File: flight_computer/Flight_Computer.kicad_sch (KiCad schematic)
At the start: 31 parts

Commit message: Update Flight_Computer.kicad_sch
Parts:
- added C?: 2.2uF, symbol Device:C
- added C? (x2): 22uF, symbol Device:C
- added D?: LED, symbol Device:LED
- added R?: 1ohm, symbol Device:R
- added R?: 1Kohm, symbol Device:R
- added R?: R, symbol Device:R
- added U?: AMS1117-3.3, Package_TO_SOT_SMD:SOT-223-3_TabPin2, symbol Regulator_Linear:AMS1117-3.3
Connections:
- net +3V3: now also C?.1, D?.2 (A), U?.2 (VO); no longer C?.1, C?.1, U?.1 (VBAT)
- net GND: now also C?.2, C?.2, R?.2, R?.2, U?.1 (GND)
- net at U?.22 (VCAP1): now also C?.2, R?.1
- net 3V3_Buck_input: no longer names the net of J?.A4 (VBUS), J?.A9 (VBUS), J?.B4 (VBUS), J?.B9 (VBUS)
- net 3V3_Buck_input: now also C?.1, U?.3 (VI)
- new net: D?.1 (K), R?.1
- new net: C?.1, R?.1, R?.2
- new net Buck_Output: C?.1, C?.1, U?.1 (VBAT)
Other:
- note added: "Find Rleak value"
- moved on the sheet: C?, Y?

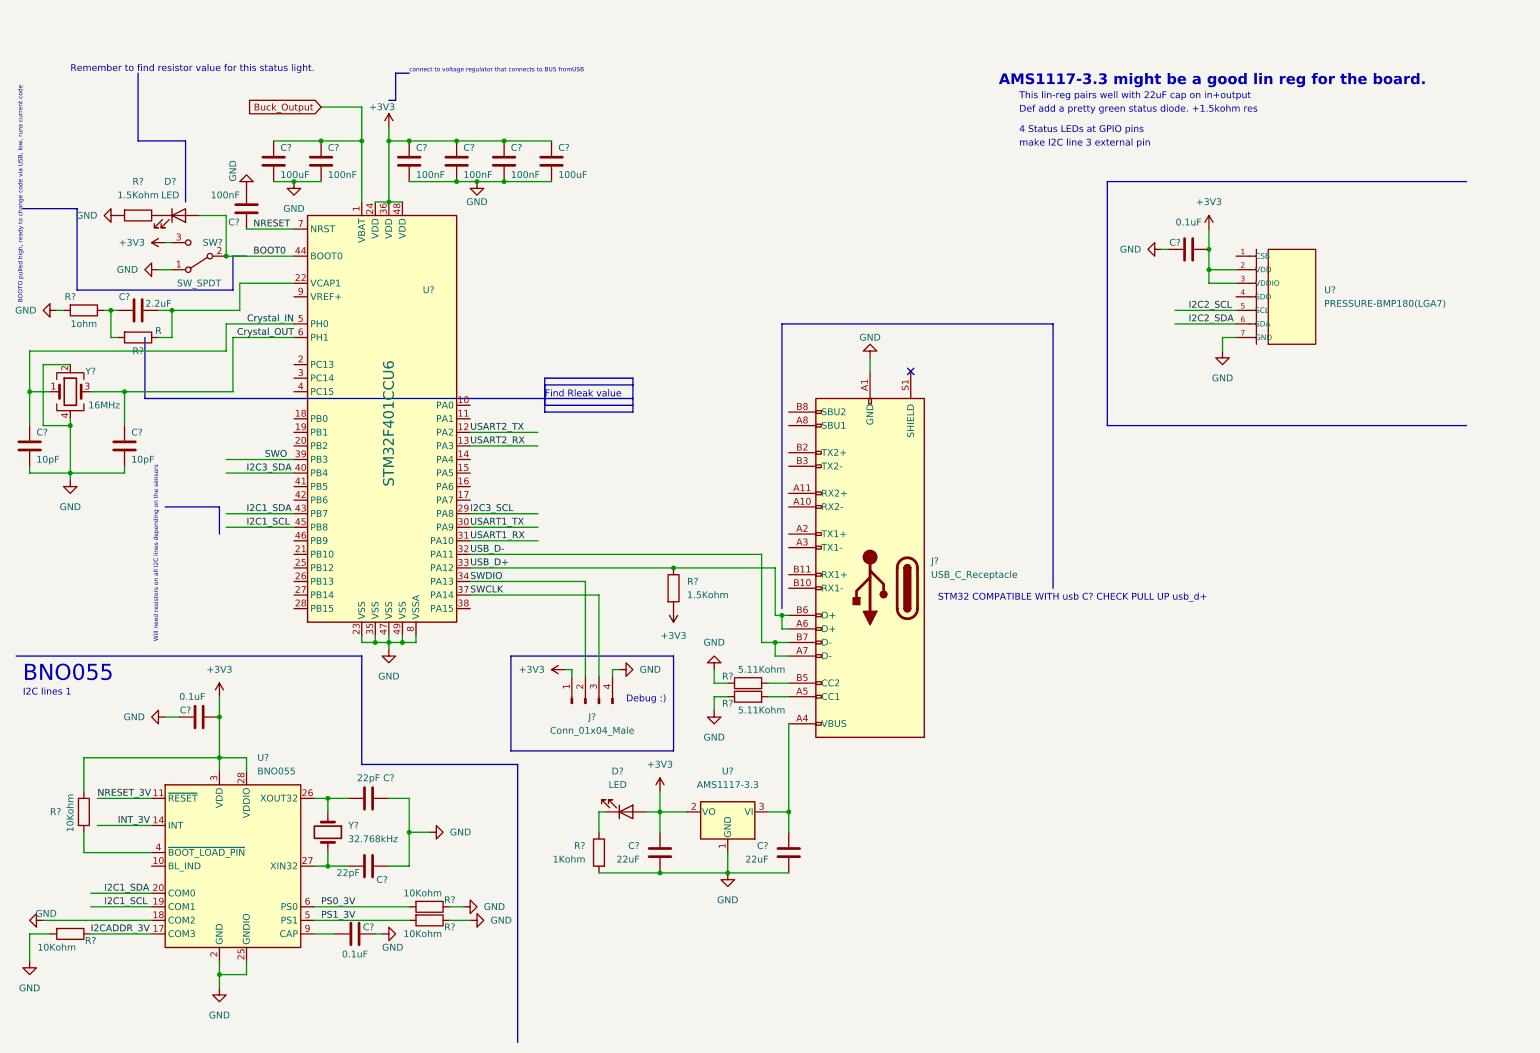
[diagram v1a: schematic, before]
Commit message: Revert "Update Flight_Computer.kicad_sch"
This reverts commit 00c3728efcfbe39ff6afe041c82bac8e4ccad5c9.
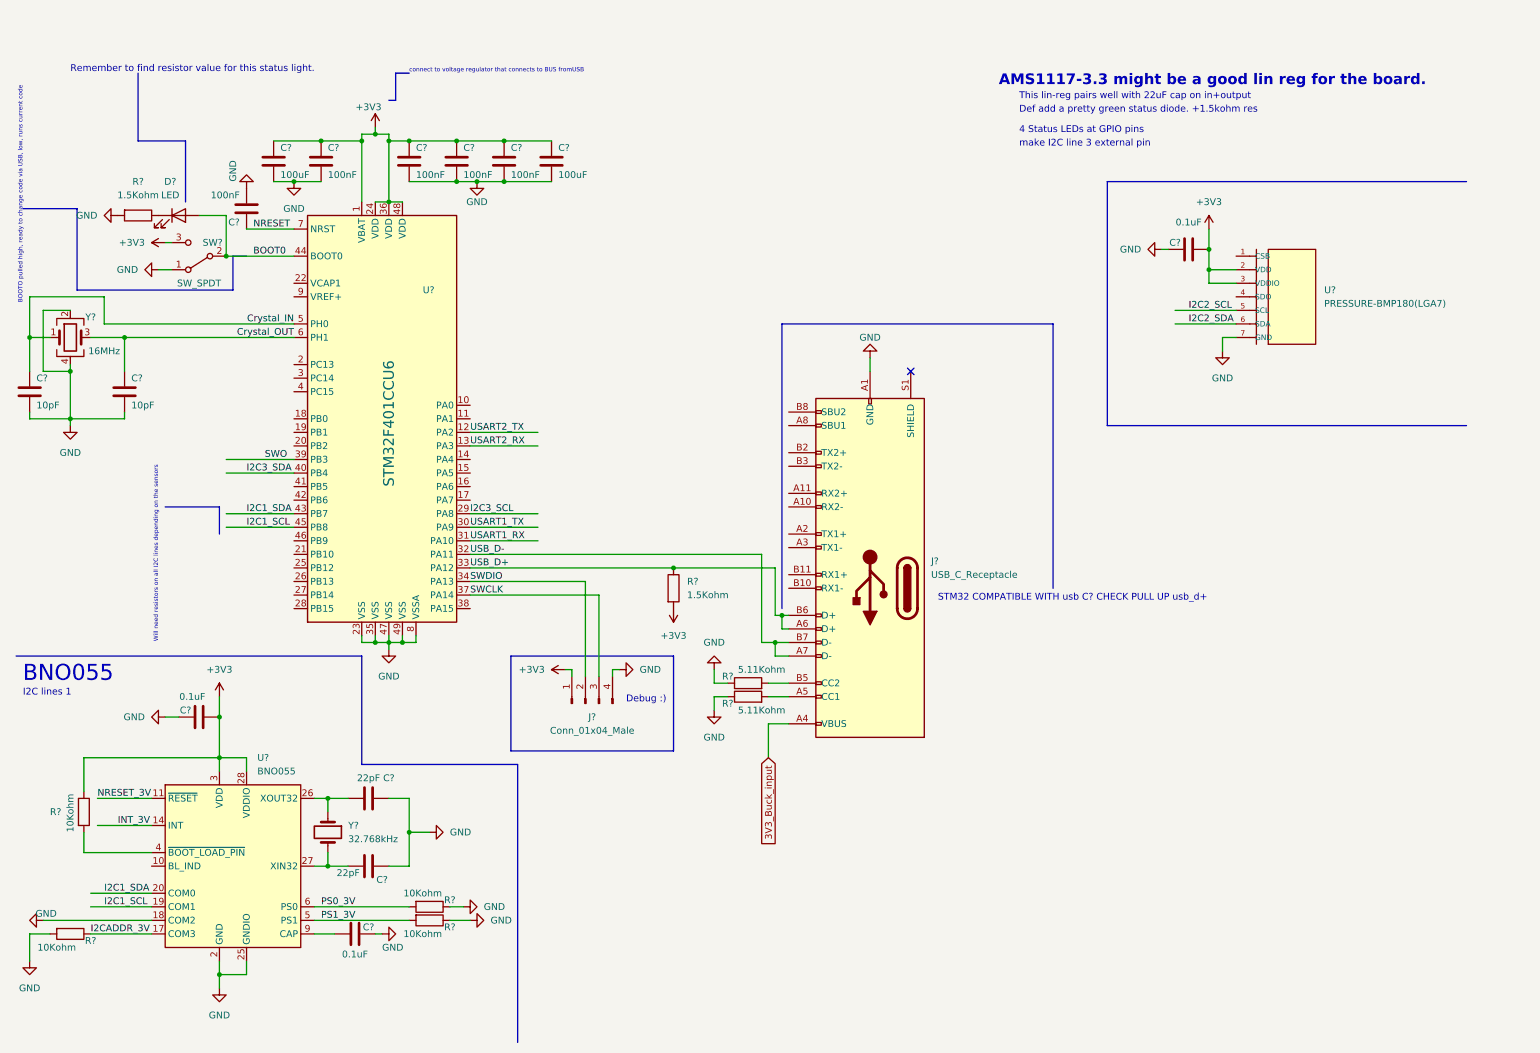
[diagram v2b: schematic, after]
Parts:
- removed C?: 2.2uF, symbol Device:C
- removed C? (x2): 22uF, symbol Device:C
- removed D?: LED, symbol Device:LED
- removed R?: 1ohm, symbol Device:R
- removed R?: 1Kohm, symbol Device:R
- removed R?: R, symbol Device:R
- removed U?: AMS1117-3.3, Package_TO_SOT_SMD:SOT-223-3_TabPin2, symbol Regulator_Linear:AMS1117-3.3
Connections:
- net Buck_Output is gone; now on net +3V3: C?.1, C?.1, U?.1 (VBAT)
- net 3V3_Buck_input: now reaches J?.A4 (VBUS), J?.A9 (VBUS), J?.B4 (VBUS), J?.B9 (VBUS)
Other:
- note removed: "Find Rleak value"
- moved on the sheet: C?, Y?

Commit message: Update Flight_Computer.kicad_sch
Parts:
- added J?: Conn_01x02_Male, symbol Connector:Conn_01x02_Male
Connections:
- net I2C3_SCL: now also J?.2 (Pin_2)
- net I2C3_SDA: now also J?.1 (Pin_1)
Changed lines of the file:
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@@
+    (stroke (width 0) (type default) (color 0 0 0 0))
+  )
+  (wire (pts (xy 111.76 92.71) (xy 111.76 97.79))
     (stroke (width 0) (type default) (color 0 0 0 0))
   )
@@
     (stroke (width 0) (type default) (color 0 0 0 0))
   )
+  (wire (pts (xy 110.49 90.17) (xy 119.38 90.17))
+    (stroke (width 0) (type default) (color 0 0 0 0))
+  )
   (wire (pts (xy 80.01 26.67) (xy 82.55 26.67))
     (stroke (width 0) (type default) (color 0 0 0 0))
@@
     (stroke (width 0) (type default) (color 0 0 0 0))
   )
+  (wire (pts (xy 119.38 92.71) (xy 111.76 92.71))
+    (stroke (width 0) (type default) (color 0 0 0 0))
+  )
   (wire (pts (xy 40.64 135.89) (xy 43.18 135.89))
     (stroke (width 0) (type default) (color 0 0 0 0))
@@
     (stroke (width 0) (type default) (color 0 0 0 0))
   )
+  (wire (pts (xy 110.49 97.79) (xy 110.49 90.17))
+    (stroke (width 0) (type default) (color 0 0 0 0))
+  )
   (wire (pts (xy 97.79 105.41) (xy 152.4 105.41))
     (stroke (width 0) (type default) (color 0 0 0 0))
@@
   )
   (wire (pts (xy 154.94 124.46) (xy 157.48 124.46))
+    (stroke (width 0) (type default) (color 0 0 0 0))
+  )
+  (wire (pts (xy 111.76 97.79) (xy 119.38 97.79))
     (stroke (width 0) (type default) (color 0 0 0 0))
   )
@@
   )
   (label "PS1_3V" (at 69.85 173.99 0)
+    (effects (font (size 1.27 1.27)) (justify left bottom))
+  )
+  (label "I2C3_SDA" (at 113.03 97.79 0)
     (effects (font (size 1.27 1.27)) (justify left bottom))
   )
@@
     (pin "2")
   )
+  (symbol (lib_id "Connector:Conn_01x02_Male") (at 124.46 92.71 180) (unit 1)
+    (in_bom yes) (on_board yes)
+    (property "Reference" "J?" (id 0) (at 124.46 87.63 0)
+      (effects (font (size 1.27 1.27)) (justify left))
+    )
+    (property "Value" "Conn_01x02_Male" (id 1) (at 138.43 91.44 0)
+      (effects (font (size 1.27 1.27)) (justify left))
+    )
+    (property "Footprint" "" (id 2) (at 124.46 92.71 0)
+      (effects (font (size 1.27 1.27)) hide)
+    )
+    (property "Datasheet" "~" (id 3) (at 124.46 92.71 0)
+      (effects (font (size 1.27 1.27)) hide)
+    )
+    (pin "1")
+    (pin "2")
+  )
   (symbol (lib_id "Device:C") (at 78.74 151.13 270) (unit 1)
     (in_bom yes) (on_board yes)
@@
       (reference "J?") (unit 1) (value "Conn_01x04_Male") (footprint "")
     )
+    (path "/bbe04b4a-dd0d-468c-a9c6-e59063d79efb"
+      (reference "J?") (unit 1) (value "Conn_01x02_Male") (footprint "")
+    )
     (path "/1f95de38-c7d1-4c35-9a65-9314a6751ee0"

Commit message: Update Flight_Computer.kicad_sch
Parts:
- added R? (x2): 10Kohm, symbol Device:R
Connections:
- net I2C3_SCL: now also R?.1; no longer J?.2 (Pin_2)
- net I2C3_SDA: now also R?.1; no longer J?.1 (Pin_1)
- new net: J?.2 (Pin_2), R?.2
- new net: J?.1 (Pin_1), R?.2
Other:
- note added: "External I2C (I2C3)"
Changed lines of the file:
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@@
+    (stroke (width 0) (type default) (color 0 0 0 0))
+  )
+  (polyline (pts (xy 110.49 86.36) (xy 138.43 86.36))
     (stroke (width 0) (type default) (color 0 0 0 0))
   )
@@
     (stroke (width 0) (type default) (color 0 0 0 0))
   )
+  (polyline (pts (xy 110.49 97.79) (xy 138.43 97.79))
+    (stroke (width 0) (type default) (color 0 0 0 0))
+  )
   (wire (pts (xy 238.76 64.77) (xy 238.76 67.31))
     (stroke (width 0) (type default) (color 0 0 0 0))
@@
     (stroke (width 0) (type default) (color 0 0 0 0))
   )
-  (wire (pts (xy 110.49 90.17) (xy 119.38 90.17))
+  (wire (pts (xy 110.49 90.17) (xy 111.76 90.17))
     (stroke (width 0) (type default) (color 0 0 0 0))
   )
@@
     (stroke (width 0) (type default) (color 0 0 0 0))
   )
-  (wire (pts (xy 119.38 92.71) (xy 111.76 92.71))
-    (stroke (width 0) (type default) (color 0 0 0 0))
-  )
   (wire (pts (xy 40.64 135.89) (xy 43.18 135.89))
     (stroke (width 0) (type default) (color 0 0 0 0))
@@
     (stroke (width 0) (type default) (color 0 0 0 0))
   )
+  (polyline (pts (xy 138.43 97.79) (xy 138.43 86.36))
+    (stroke (width 0) (type default) (color 0 0 0 0))
+  )
   (wire (pts (xy 152.4 121.92) (xy 154.94 121.92))
     (stroke (width 0) (type default) (color 0 0 0 0))
@@
   )
   (wire (pts (xy 80.01 121.92) (xy 82.55 121.92))
+    (stroke (width 0) (type default) (color 0 0 0 0))
+  )
+  (polyline (pts (xy 110.49 86.36) (xy 110.49 97.79))
     (stroke (width 0) (type default) (color 0 0 0 0))
   )
@@
   (text "BNO055" (at 13.97 129.54 0)
     (effects (font (size 3 3)) (justify left bottom))
+  )
+  (text "External I2C (I2C3)" (at 119.38 86.36 0)
+    (effects (font (size 1.27 1.27)) (justify left bottom))
   )
   (text "4 Status LEDs at GPIO pins" (at 200.66 26.67 0)
@@
     (pin "1")
   )
+  (symbol (lib_id "Device:R") (at 115.57 90.17 90) (unit 1)
+    (in_bom yes) (on_board yes)
+    (property "Reference" "R?" (id 0) (at 119.38 88.9 90))
+    (property "Value" "10Kohm" (id 1) (at 115.57 87.63 90)
+      (effects (font (size 1 1)))
+    )
+    (property "Footprint" "" (id 2) (at 115.57 91.948 90)
+      (effects (font (size 1.27 1.27)) hide)
+    )
+    (property "Datasheet" "~" (id 3) (at 115.57 90.17 0)
+      (effects (font (size 1.27 1.27)) hide)
+    )
+    (pin "1")
+    (pin "2")
+  )
   (symbol (lib_id "Device:C") (at 69.85 31.75 0) (unit 1)
     (in_bom yes) (on_board yes)
@@
     (pin "1")
   )
+  (symbol (lib_id "Device:R") (at 115.57 92.71 90) (unit 1)
+    (in_bom yes) (on_board yes)
+    (property "Reference" "R?" (id 0) (at 119.38 93.98 90))
+    (property "Value" "10Kohm" (id 1) (at 115.57 95.25 90)
+      (effects (font (size 1 1)))
+    )
+    (property "Footprint" "" (id 2) (at 115.57 94.488 90)
+      (effects (font (size 1.27 1.27)) hide)
+    )
+    (property "Datasheet" "~" (id 3) (at 115.57 92.71 0)
+      (effects (font (size 1.27 1.27)) hide)
+    )
+    (pin "1")
+    (pin "2")
+  )
   (symbol (lib_id "Device:C") (at 113.03 31.75 0) (unit 1)
     (in_bom yes) (on_board yes)
@@
       (reference "R?") (unit 1) (value "10Kohm") (footprint "")
     )
+    (path "/90af90e9-a9bc-4dfa-a8bb-2923cb87a756"
+      (reference "R?") (unit 1) (value "10Kohm") (footprint "")
+    )
     (path "/bb53ed2f-610f-4747-9474-3229a6acbd67"
       (reference "R?") (unit 1) (value "1.5Kohm") (footprint "")
@@
       (reference "R?") (unit 1) (value "1.5Kohm") (footprint "")
     )
+    (path "/f57704ef-1403-424d-8e91-ba7088b89e39"
+      (reference "R?") (unit 1) (value "10Kohm") (footprint "")
+    )
     (path "/d8996dea-e451-4b97-864d-dc590f430ce3"
